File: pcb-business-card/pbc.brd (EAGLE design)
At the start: 50 x 88 mm, 29 parts, among them IC1 NET2272REV1A-BCF, J1 CON2, U1 MEGA32U4-MU, U2 RT9193-33GB, U5 TMP117AIYBGR

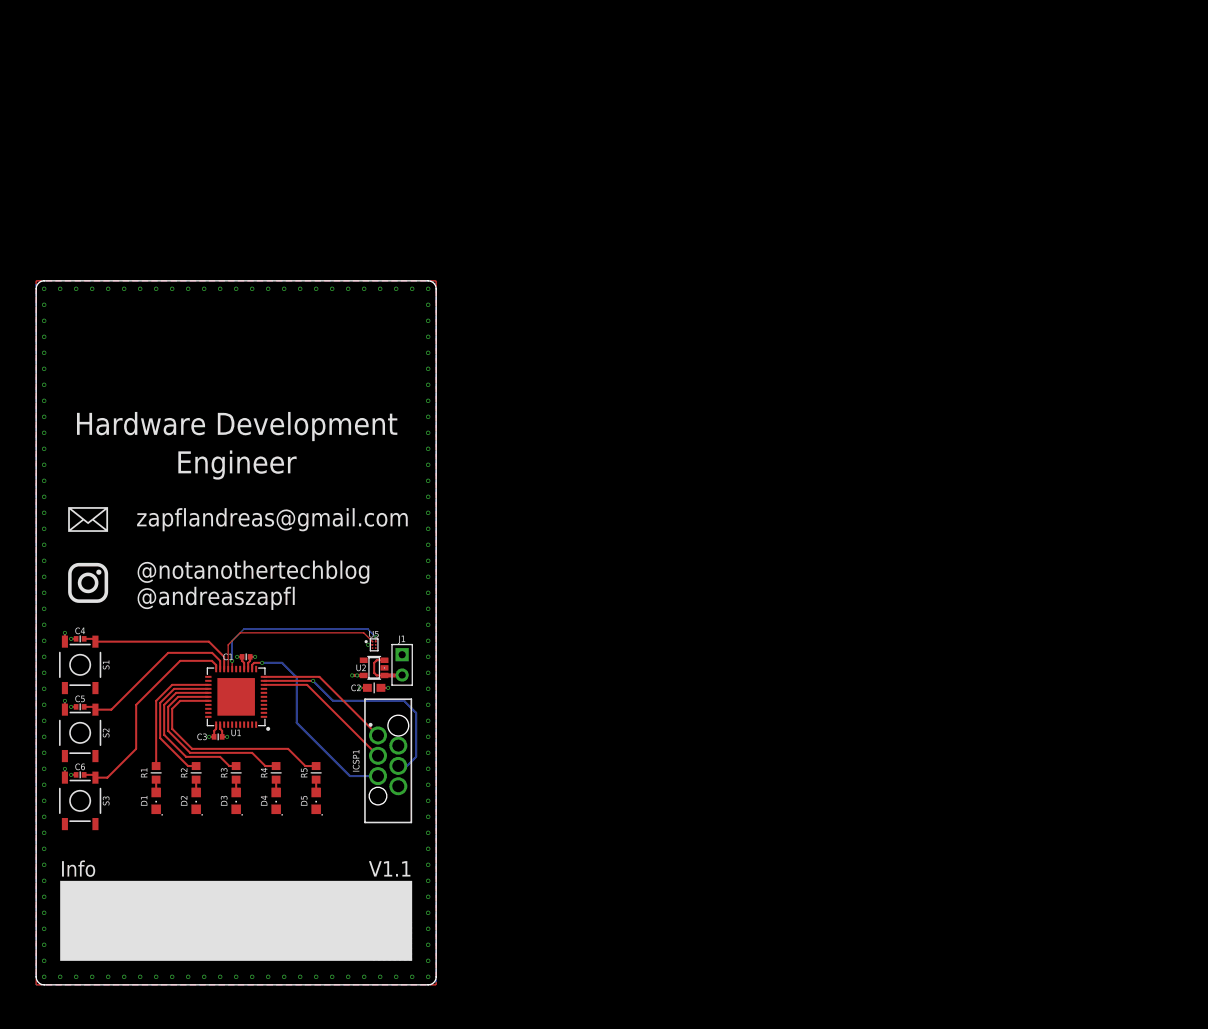
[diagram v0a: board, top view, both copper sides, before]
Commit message: Updated format to id-1 size
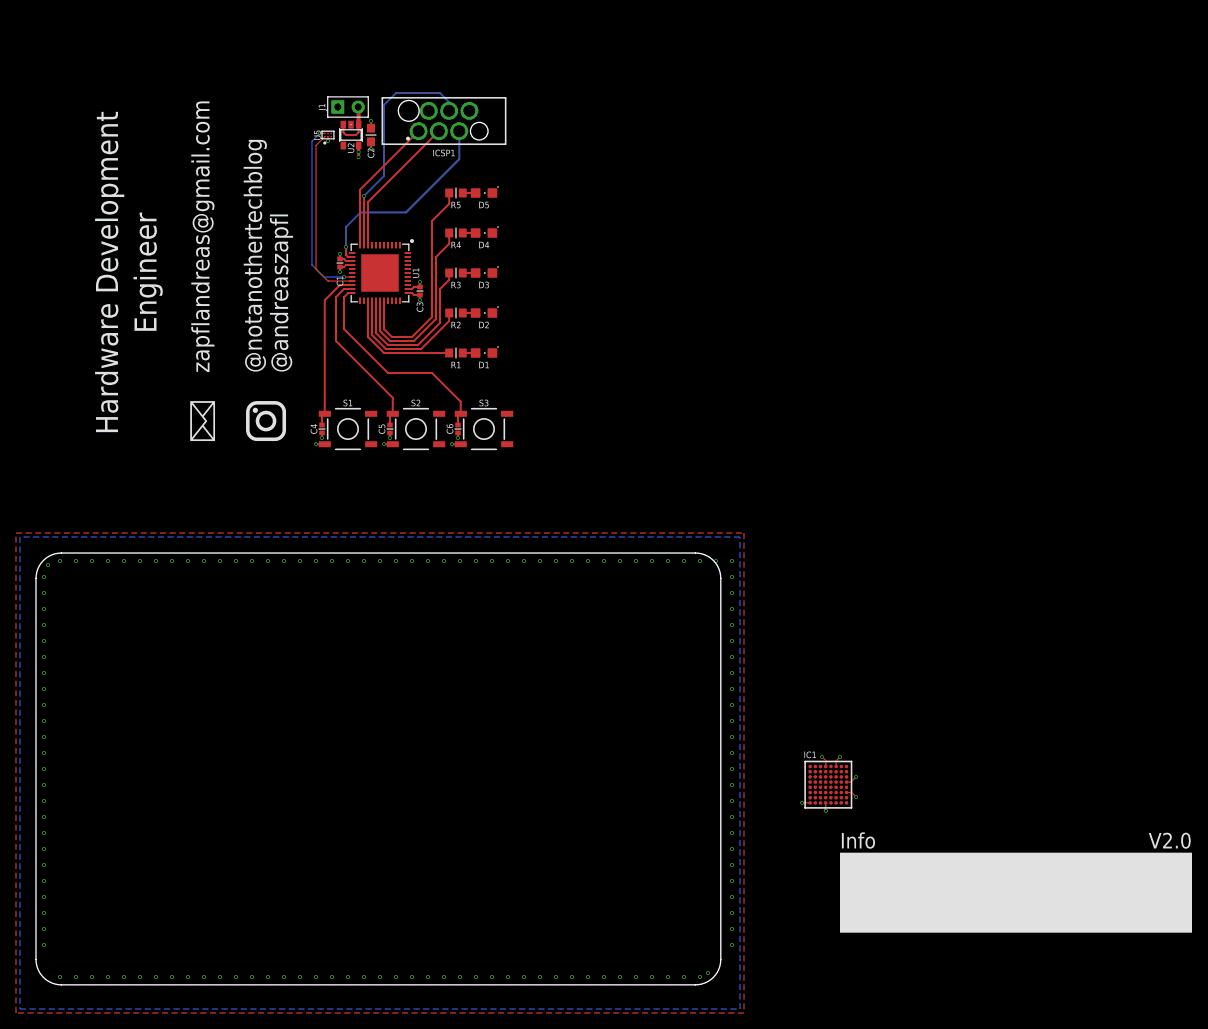
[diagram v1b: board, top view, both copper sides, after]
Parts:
- moved ICSP1 80.3 mm to (51.0, 108.0), turned to 180 degrees
- moved D5 78.8 mm to (56.0, 99.0), turned to 270 degrees
- moved D4 75.6 mm to (56.0, 94.0), turned to 270 degrees
- moved R5 74.6 mm to (52.5, 99.0), turned to 180 degrees
- moved D3 72.9 mm to (56.0, 89.0), turned to 270 degrees
- moved R4 71.1 mm to (52.5, 94.0), turned to 180 degrees
- moved D2 70.8 mm to (56.0, 84.0), turned to 270 degrees
- moved J1 70.1 mm to (39.0, 109.7), turned to 90 degrees
- moved D1 69.4 mm to (56.0, 79.0), turned to 270 degrees
- moved C2 69.1 mm to (41.9, 106.2), turned to 90 degrees
- moved S3 68.6 mm to (56.0, 69.5), turned to 180 degrees
- moved R3 68.3 mm to (52.5, 89.0), turned to 180 degrees
- moved U2 66.7 mm to (39.4, 106.2), turned to 180 degrees
- moved R2 66.0 mm to (52.5, 84.0), turned to 180 degrees
- moved R1 64.5 mm to (52.5, 79.0), turned to 180 degrees
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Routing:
- net VSSIO: track 0.00 -> 3.42 mm, vias 0 -> 3
- net GND: track 10.9 -> 13.7 mm, vias 143 -> 145
- net VSSC: track 0.00 -> 1.48 mm, vias 0 -> 1
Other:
- board size 50 x 88 mm -> 85.6 x 54 mm
- board text added: "ID-1: 85.6 x 53.98 mm, Radius: 3.175 mm"
- board text added: "V2.0"
- board text removed: "V1.1"

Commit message: Working on verion 2
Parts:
- added U$5: (no value), EET-Symbols:STACKUP-2L
- added U$6: (no value), EET-Symbols:QR-SPACE
- moved U$4 69.8 mm to (17.0, 17.0), turned to 90 degrees
- moved U$2 63.7 mm to (5.48, 9.77), turned to 0 degrees
- moved U$3 52.4 mm to (5.48, 18.4), turned to 0 degrees
- moved IC1 43.8 mm to (57.5, 39.0)

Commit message: Working on version 2
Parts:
- moved U$6 48.7 mm to (77.0, 14.0)
- moved U$5 15.7 mm to (65.5, 47.2)
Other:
- outline, holes or cut-outs redrawn
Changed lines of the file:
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@@
 <wire x1="0" y1="0" x2="85.58" y2="53.98" width="0.2" layer="51"/>
 <wire x1="0" y1="54" x2="85.58" y2="0.02" width="0.2" layer="52"/>
+<hole x="80.5" y="49" drill="3.175"/>
+<wire x1="77.5" y1="6" x2="77.5" y2="5" width="0" layer="20" curve="180"/>
+<wire x1="77.5" y1="5" x2="82" y2="5" width="0" layer="20"/>
+<wire x1="82" y1="5" x2="82.5" y2="5.5" width="0" layer="20" curve="90"/>
+<wire x1="82.5" y1="5.5" x2="82.5" y2="10.5" width="0" layer="20"/>
+<wire x1="82.5" y1="10.5" x2="81.5" y2="10.5" width="0" layer="20" curve="180"/>
+<wire x1="81.5" y1="10.5" x2="81.5" y2="6" width="0" layer="20"/>
+<wire x1="81.5" y1="6" x2="77.5" y2="6" width="0" layer="20"/>
+<circle x="82" y="10.5" radius="0.5" width="0" layer="51"/>
 </plain>
 <attributes>
@@
 <element name="U$3" library="zaan-Symbols" library_urn="urn:adsk.eagle:library:16759578" package="MAIL-5" value="" x="5.48" y="18.395" smashed="yes"/>
 <element name="U$2" library="zaan-Symbols" library_urn="urn:adsk.eagle:library:16759578" package="INSTA-5" value="" x="5.48" y="9.77" smashed="yes"/>
-<element name="U$5" library="EET-Symbols" package="STACKUP-2L" value="" x="60" y="62" smashed="yes"/>
-<element name="U$6" library="EET-Symbols" package="QR-SPACE" value="" x="68.5" y="62" smashed="yes"/>
+<element name="U$5" library="EET-Symbols" package="STACKUP-2L" value="" x="65.5" y="47.25" smashed="yes"/>
+<element name="U$6" library="EET-Symbols" package="QR-SPACE" value="" x="77" y="14" smashed="yes"/>
 </elements>
 <signals>

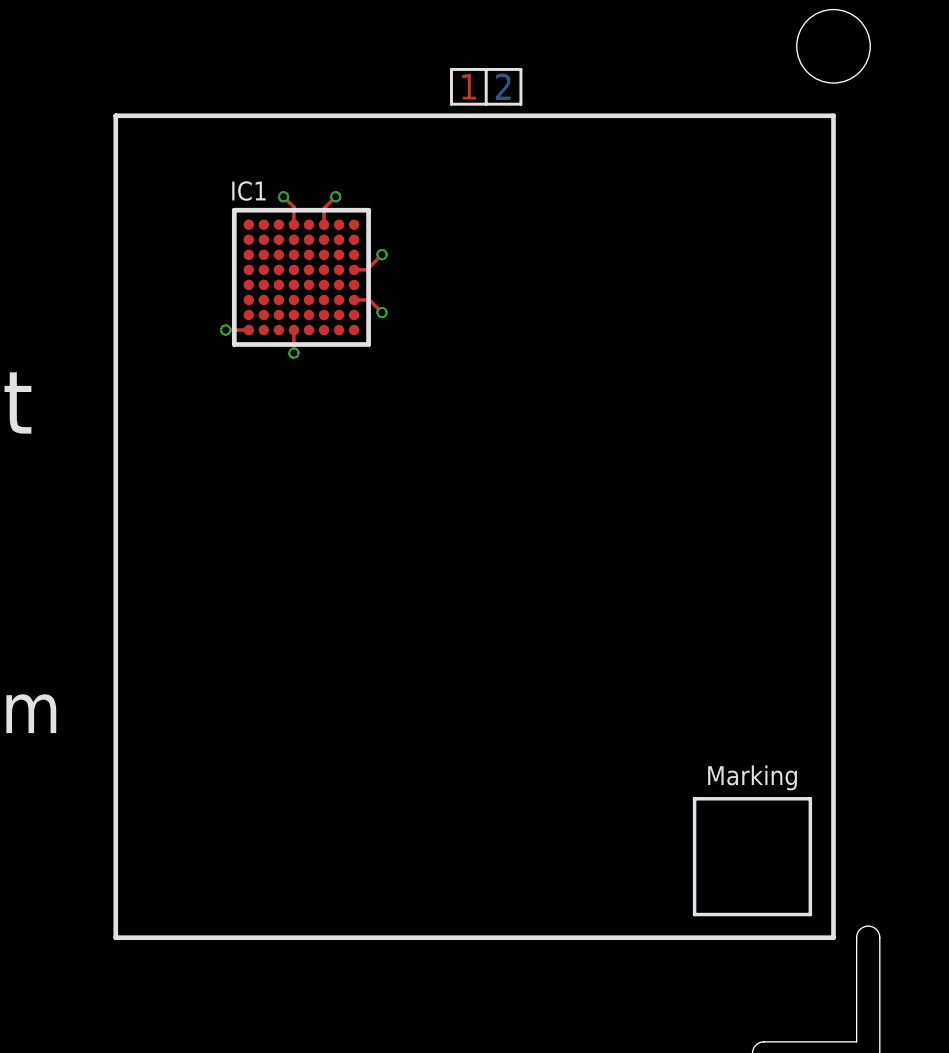
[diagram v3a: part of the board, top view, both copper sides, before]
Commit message: Added TP and FID
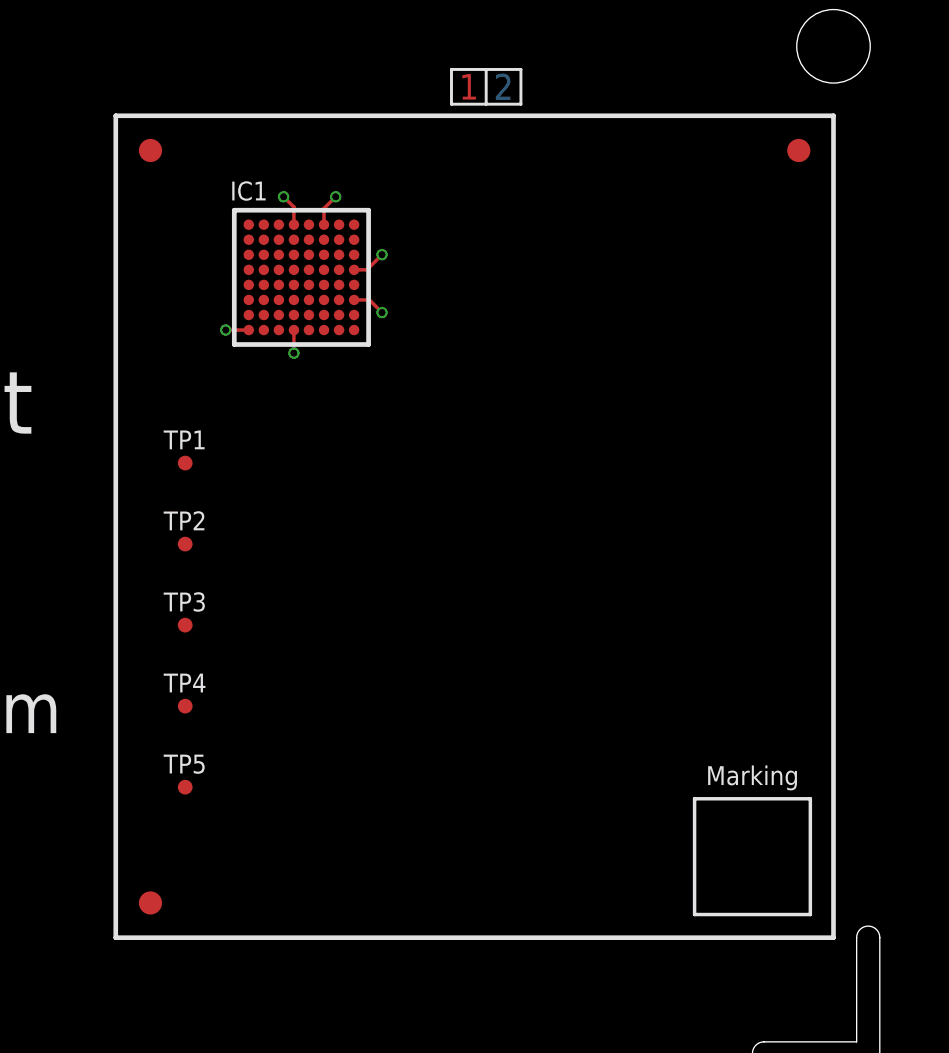
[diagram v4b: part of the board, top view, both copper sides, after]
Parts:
- added FD1, FD2, FD3: FIDUCIAL, EET-Symbols:FIDUCIAL_1MM
- added TP1, TP2, TP3, TP4, TP5: TP-B0.635, EET-No-Category:B0.635
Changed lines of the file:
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@@
 <element name="U$5" library="EET-Symbols" package="STACKUP-2L" value="" x="65.5" y="47.25" smashed="yes"/>
 <element name="U$6" library="EET-Symbols" package="QR-SPACE" value="" x="77" y="14" smashed="yes"/>
+<element name="TP1" library="EET-No-Category" package="B0.635" value="TP-B0.635" x="52.5" y="31" smashed="yes">
+<attribute name="NAME" x="52.5" y="32" size="0.8128" layer="25" font="vector" ratio="15" align="center"/>
+<attribute name="TP_SIGNAL_NAME" value="" x="52.5" y="31" size="1.778" layer="27" display="off"/>
+<attribute name="VALUE" x="51.865" y="30.238" size="0.0254" layer="27"/>
+</element>
+<element name="TP2" library="EET-No-Category" package="B0.635" value="TP-B0.635" x="52.5" y="27.5" smashed="yes">
+<attribute name="NAME" x="52.5" y="28.5" size="0.8128" layer="25" font="vector" ratio="15" align="center"/>
+<attribute name="TP_SIGNAL_NAME" value="" x="52.5" y="27.5" size="1.778" layer="27" display="off"/>
+<attribute name="VALUE" x="51.865" y="26.738" size="0.0254" layer="27"/>
+</element>
+<element name="TP3" library="EET-No-Category" package="B0.635" value="TP-B0.635" x="52.5" y="24" smashed="yes">
+<attribute name="NAME" x="52.5" y="25" size="0.8128" layer="25" font="vector" ratio="15" align="center"/>
+<attribute name="TP_SIGNAL_NAME" value="" x="52.5" y="24" size="1.778" layer="27" display="off"/>
+<attribute name="VALUE" x="51.865" y="23.238" size="0.0254" layer="27"/>
+</element>
+<element name="TP4" library="EET-No-Category" package="B0.635" value="TP-B0.635" x="52.5" y="20.5" smashed="yes">
+<attribute name="NAME" x="52.5" y="21.5" size="0.8128" layer="25" font="vector" ratio="15" align="center"/>
+<attribute name="TP_SIGNAL_NAME" value="" x="52.5" y="20.5" size="1.778" layer="27" display="off"/>
+<attribute name="VALUE" x="51.865" y="19.738" size="0.0254" layer="27"/>
+</element>
+<element name="TP5" library="EET-No-Category" package="B0.635" value="TP-B0.635" x="52.5" y="17" smashed="yes">
+<attribute name="NAME" x="52.5" y="18" size="0.8128" layer="25" font="vector" ratio="15" align="center"/>
+<attribute name="TP_SIGNAL_NAME" value="" x="52.5" y="17" size="1.778" layer="27" display="off"/>
+<attribute name="VALUE" x="51.865" y="16.238" size="0.0254" layer="27"/>
+</element>
+<element name="FD1" library="EET-Symbols" package="FIDUCIAL_1MM" package3d_urn="urn:adsk.eagle:package:25891413/2" value="FIDUCIAL" x="51" y="44.5" smashed="yes" rot="R90"/>
+<element name="FD2" library="EET-Symbols" package="FIDUCIAL_1MM" package3d_urn="urn:adsk.eagle:package:25891413/2" value="FIDUCIAL" x="79" y="44.5" smashed="yes" rot="R90"/>
+<element name="FD3" library="EET-Symbols" package="FIDUCIAL_1MM" package3d_urn="urn:adsk.eagle:package:25891413/2" value="FIDUCIAL" x="51" y="12" smashed="yes" rot="R90"/>
 </elements>
 <signals>
@@
 <wire x1="52.98" y1="52.98" x2="53.08" y2="67.575" width="0" layer="19" extent="1-1"/>
 <wire x1="84.98" y1="52.98" x2="82.98" y2="52.98" width="0" layer="19" extent="1-1"/>
-<wire x1="56.75" y1="42.5" x2="86.98" y2="28.98" width="0" layer="19" extent="1-1"/>
-<wire x1="58.495" y1="41.295" x2="57.195" y2="41.295" width="0" layer="19" extent="1-1"/>
 </signal>
 <signal name="VCC">
